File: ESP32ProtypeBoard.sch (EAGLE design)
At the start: 103 parts, among them IC1 SOIC-8, IC2 SI4431BDY, IC4 LMC555*, J10 POWER_JACKPTH_LOCK, Q1 MMBT3904*, Q2 MMBT3904, Q3 MMBT3904, U2 ESP-WROOM-32

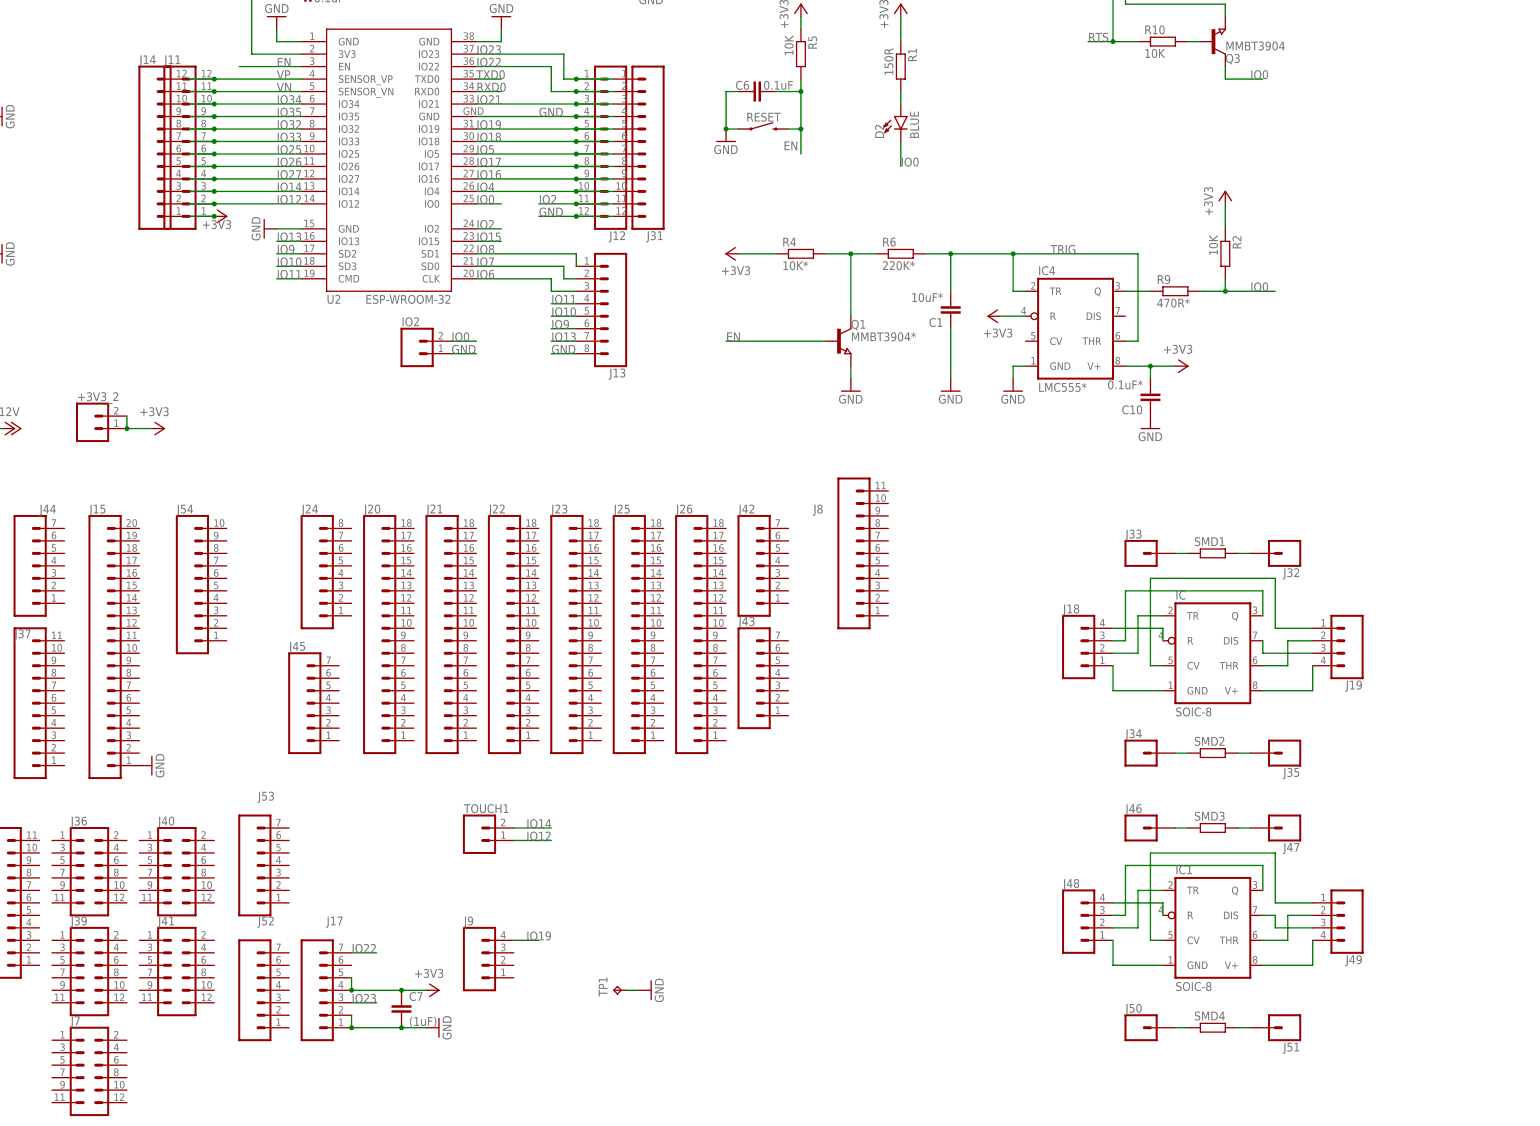
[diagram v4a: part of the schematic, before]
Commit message: Schema reordered for easier reuse
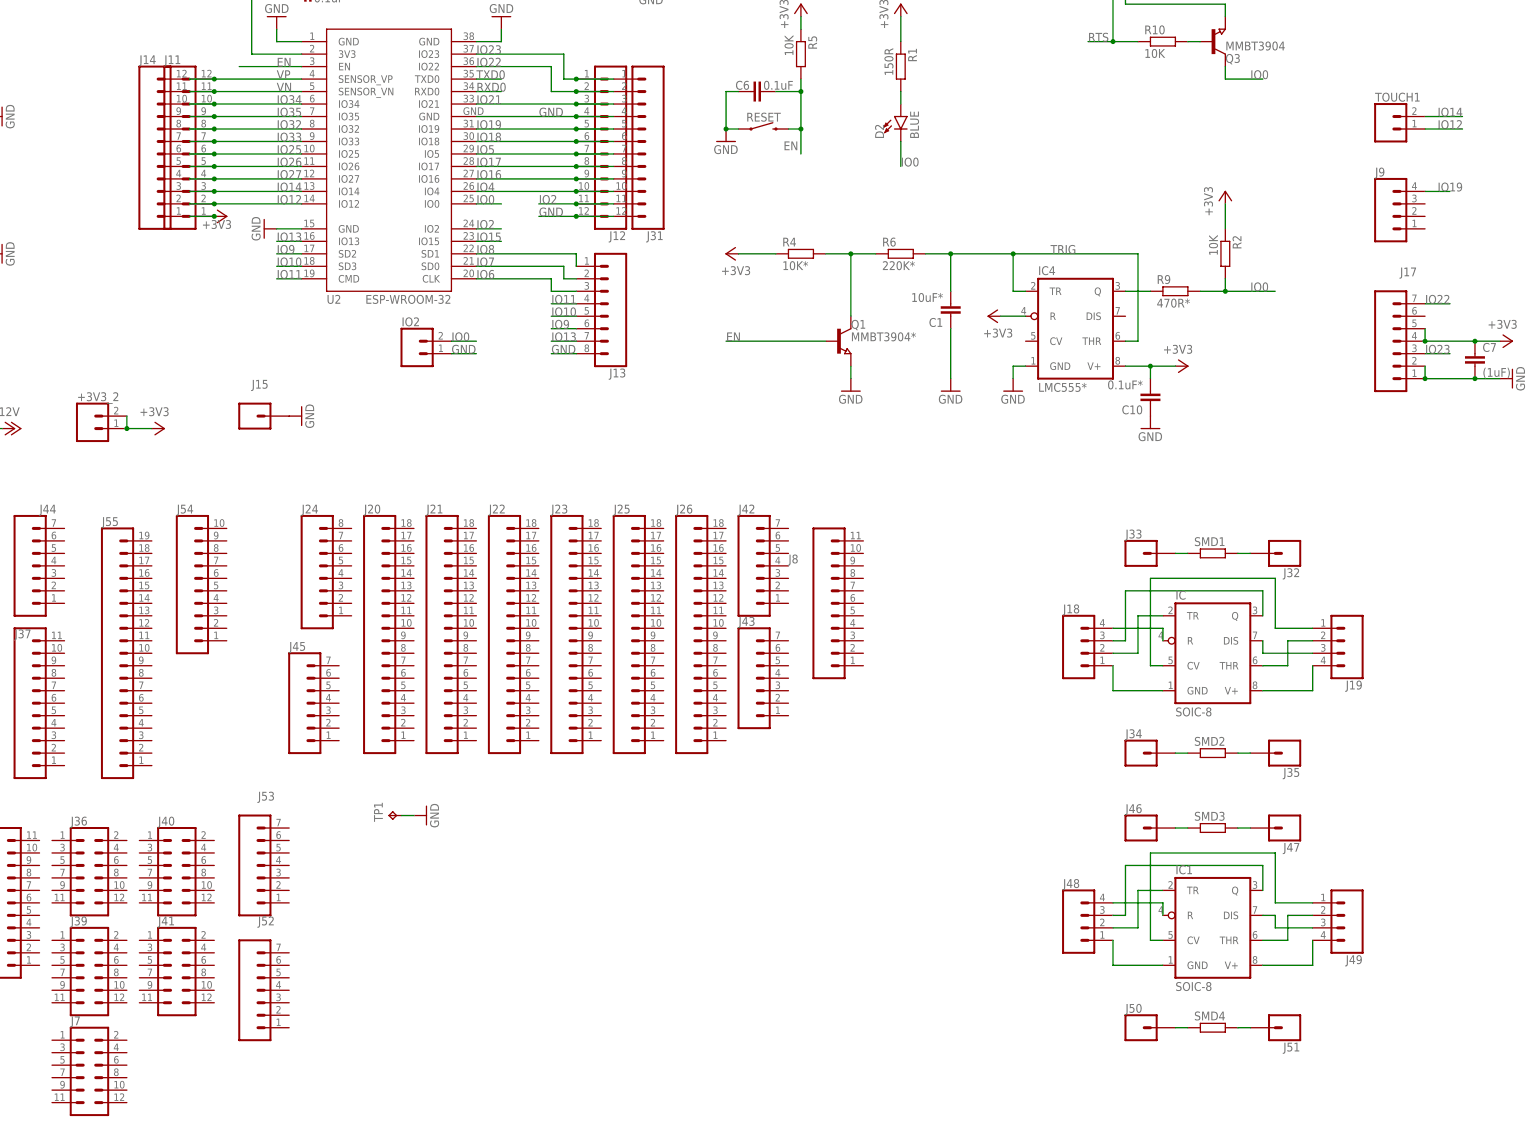
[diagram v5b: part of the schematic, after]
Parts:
- added J55: (no value), SparkFun-Connectors:CONN_191X19_NO_SILK
- J15: device SparkFun-Connectors:CONN_20NOSILK -> SparkFun-Connectors:CONN_01PTH_NO_SILK_KIT
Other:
- moved on the sheet: C7, J17, J8, J9, TOUCH1, TP1

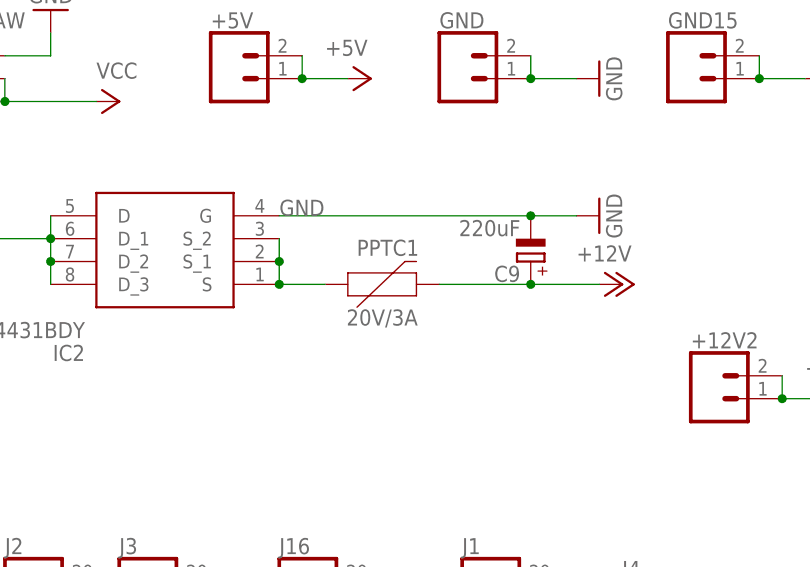
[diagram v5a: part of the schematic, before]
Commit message: Removed main fuse
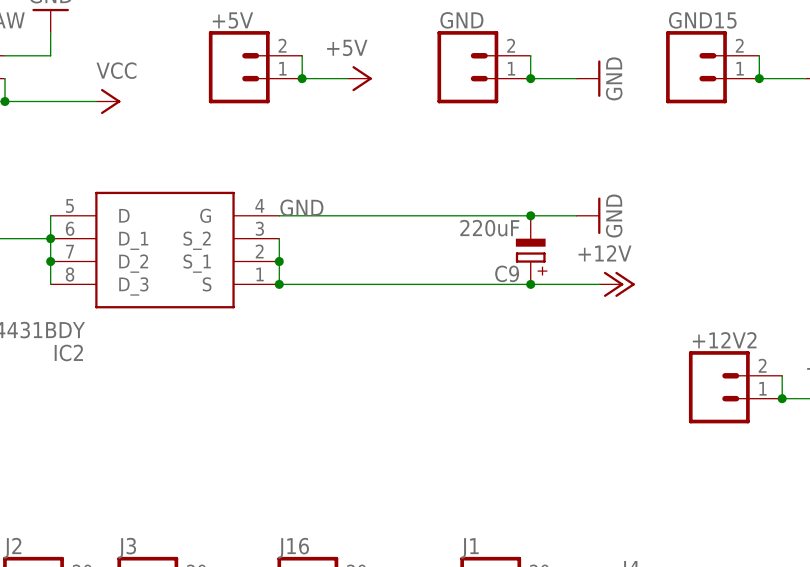
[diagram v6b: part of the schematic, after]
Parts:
- removed PPTC1: 20V/3A, SparkFun-Fuses:PPTC_PTH
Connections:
- removed net N$31: IC2.S, IC2.S_1, IC2.S_2, PPTC1.1
- net +12V: now also IC2.S, IC2.S_1, IC2.S_2; no longer PPTC1.2
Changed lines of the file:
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@@
 <part name="R2" library="eagle-ltspice" library_urn="urn:adsk.eagle:library:217" deviceset="R" device="R1206" package3d_urn="urn:adsk.eagle:package:13301/1" value="10K"/>
 <part name="+3V2" library="supply1" library_urn="urn:adsk.eagle:library:371" deviceset="+3V3" device=""/>
-<part name="PPTC1" library="SparkFun-Fuses" deviceset="PPTC" device="_PTH" value="20V/3A"/>
 <part name="P+11" library="supply1" library_urn="urn:adsk.eagle:library:371" deviceset="VCC" device=""/>
 <part name="+3V8" library="supply1" library_urn="urn:adsk.eagle:library:371" deviceset="+3V3" device=""/>
@@
 <instance part="+3V2" gate="G$1" x="368.3" y="48.26" smashed="yes">
 <attribute name="VALUE" x="365.76" y="43.18" size="1.778" layer="96" rot="R90"/>
-</instance>
-<instance part="PPTC1" gate="F1" x="68.58" y="12.7" smashed="yes">
-<attribute name="NAME" x="70.485" y="15.875" size="1.778" layer="95" font="vector" align="bottom-center"/>
-<attribute name="VALUE" x="69.85" y="9.906" size="1.778" layer="96" font="vector" align="top-center"/>
 </instance>
 <instance part="P+11" gate="VCC" x="20.32" y="17.78" smashed="yes" rot="R90">
@@
 <junction x="86.36" y="12.7"/>
 <pinref part="P+4" gate="1" pin="+12V"/>
-<pinref part="PPTC1" gate="F1" pin="2"/>
-<wire x1="86.36" y1="12.7" x2="76.2" y2="12.7" width="0.1524" layer="91"/>
+<pinref part="IC2" gate="G$1" pin="S"/>
+<pinref part="IC2" gate="G$1" pin="S_1"/>
+<pinref part="IC2" gate="G$1" pin="S_2"/>
+<wire x1="58.42" y1="17.78" x2="58.42" y2="15.24" width="0.1524" layer="91"/>
+<junction x="58.42" y="15.24"/>
+<wire x1="58.42" y1="15.24" x2="58.42" y2="12.7" width="0.1524" layer="91"/>
+<junction x="58.42" y="12.7"/>
+<wire x1="58.42" y1="12.7" x2="86.36" y2="12.7" width="0.1524" layer="91"/>
 </segment>
 <segment>
@@
 </segment>
 </net>
-<net name="N$31" class="0">
-<segment>
-<pinref part="IC2" gate="G$1" pin="S"/>
-<pinref part="IC2" gate="G$1" pin="S_1"/>
-<pinref part="IC2" gate="G$1" pin="S_2"/>
-<wire x1="58.42" y1="17.78" x2="58.42" y2="15.24" width="0.1524" layer="91"/>
-<junction x="58.42" y="15.24"/>
-<wire x1="58.42" y1="15.24" x2="58.42" y2="12.7" width="0.1524" layer="91"/>
-<junction x="58.42" y="12.7"/>
-<pinref part="PPTC1" gate="F1" pin="1"/>
-<wire x1="63.5" y1="12.7" x2="58.42" y2="12.7" width="0.1524" layer="91"/>
-</segment>
-</net>

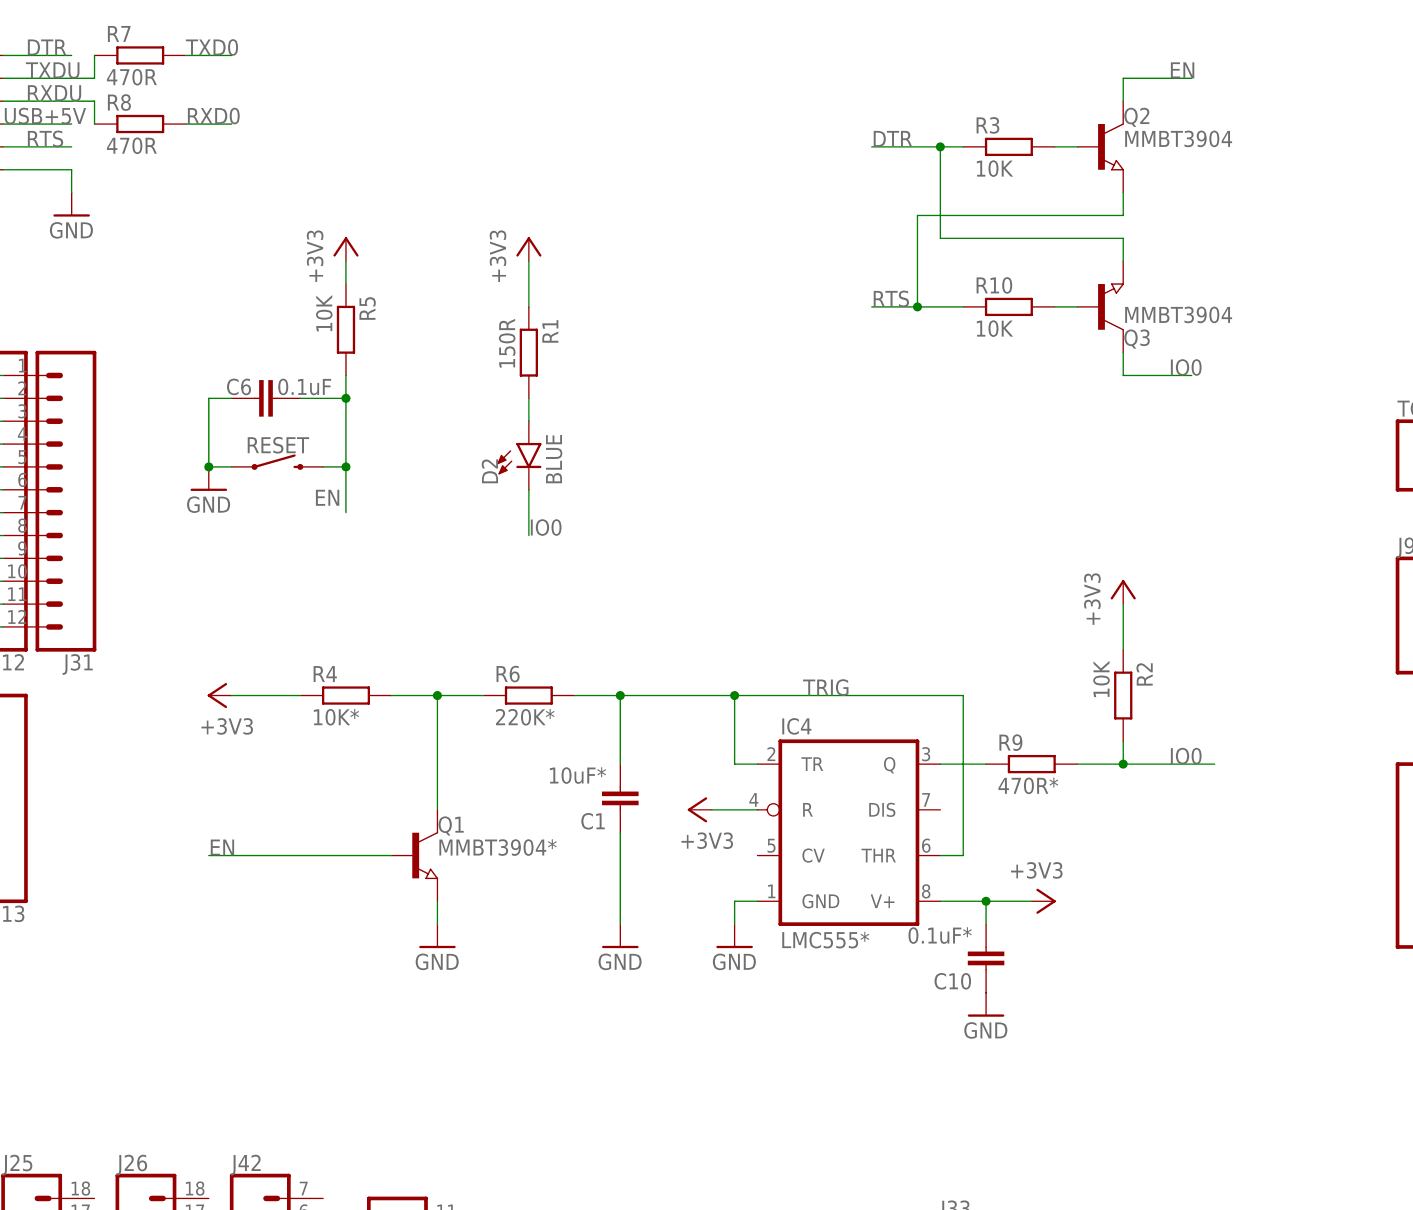
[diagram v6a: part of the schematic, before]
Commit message: Removed long-press flash mode
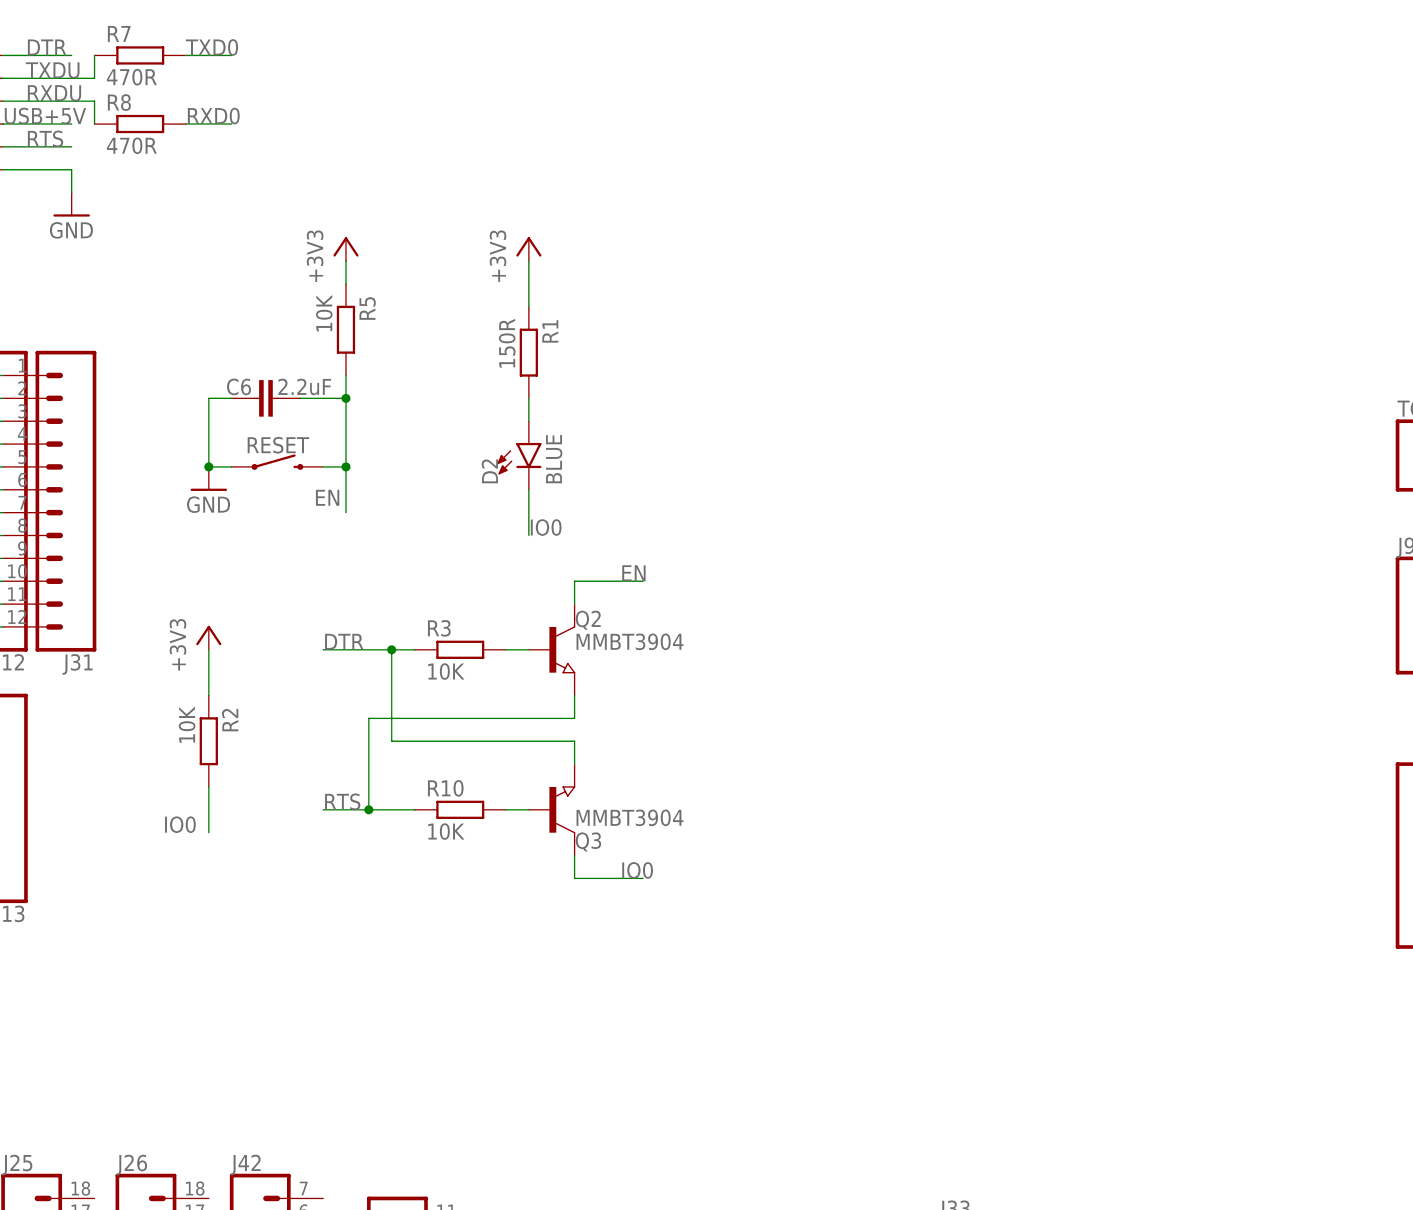
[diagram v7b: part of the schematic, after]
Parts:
- removed C1: 10uF*, rcl:C-EUC1206
- removed C10: 0.1uF*, rcl:C-EUC1206
- removed IC4: LMC555*, linear:LM555D
- removed Q1: MMBT3904*, semicon-smd-ipc:NPN-TRANSISTOR_SOT23
- removed R4: 10K*, eagle-ltspice:RR1206
- removed R6: 220K*, eagle-ltspice:RR1206
- removed R9: 470R*, eagle-ltspice:RR1206
- C6: value 0.1uF -> 2.2uF
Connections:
- removed net AUTO_FLASH: IC4.Q, R9.1
- removed net Q1C: Q1.C, R4.2, R6.1
- removed net TRIG: C1.2, IC4.THR, IC4.TR, R6.2
- net +3V3: no longer C10.2, IC4.R, IC4.V+, R4.1
- net EN: no longer Q1.B
- net GND: no longer C1.1, C10.1, IC4.GND, Q1.E
- net IO0: no longer R9.2
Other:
- moved on the sheet: Q2, Q3, R10, R2, R3
